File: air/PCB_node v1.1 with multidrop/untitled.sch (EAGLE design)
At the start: 100 parts, among them J1 10118193-0001LF, J2 10118193-0001LF, K1 351, K2 351, K3 SRD-05VDC-SL-C, Q1 MMBT3904, Q2 MMBT3904, Q3 12MHz, Q4 S9013, Q5 S9013, Q6 S9013, Q7 12MHz, Q8 MMBT3904, Q9 MMBT3904, U1 CH340G, U10 ADS1115IDGSR, U2 ESP32-WROOM-32D, U3 AMS1117, U4 PC817X2NIP0F, U5 PC817X2NIP0F, U6 PC817X2NIP0F, U7 CH340G, U8 AMS1117, U9 ESP32-WROOM-32D, X1 MSTBA2, X2 MSTBA2, X3 MSTBA4, X4 MSTBA3, X5 MSTBA2, X6 MSTBA4, X7 C-GRID-02-70543

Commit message: PCB dasmeter dengan multidop
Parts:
- added D13, D14, D15: US1M-13, US1M-13:US1M-13
- added K4: 351, relay:351
- added Q10: S9013, S9013:S9013
- added R21, R9: (no value), rcl:R-EU_0207/12
- added R22: 1k, rcl:R-US_M0805
- added R29, R31: 10k, rcl:R-US_M0805
- added R30: 560, rcl:R-US_M0805
- added U11: PC817X2NIP0F, PC817X2NIP0F:PC817X2NIP0F
- added X8: MSTBA2, con-phoenix-508:MSTBA2
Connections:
- removed net 24V++: K3.NO, R15.2, SUPER-STEPDOWN1.IN+, X2-2.1
- removed net M0: EBYTEE220-900T22D1.M0, EBYTEE220-900T22D1.M1, U2.IO18
- new net GND-BATT: K3.NO, X1-2.1, X2-1.1
- new net M1: EBYTEE220-900T22D1.M1, U9.IO5
- new net M2_RX: D14.A, K43.P, R30.2
- new net M2_SWITCHGPS: R22.2, U9.IO26
- new net M2_TX: K42.P, U9.IO16
- new net N$30: R22.1, U11.A
- new net N$31: Q10.B, U11.ET
- new net N$32: R29.2, U11.CT
- new net N$33: D13.A, K41.2, Q10.C
- new net N$34: D14.K, U9.IO17
- new net N$35: D15.K, U2.IO17
- new net PB-PWR: R9.2, X3-3.1
- net 24V+: now also R15.2, SUPER-STEPDOWN1.IN+, X1-1.1; no longer K3.COM, X1-2.1, X2-1.1
- net CONFIG_LORA: now also U9.IO25; no longer U2.IO5
- net CYBLE3: now also R21.2, R9.1; no longer X3-3.1
- net GND: now also EBYTEE220-900T22D1.M0, K3.COM, Q10.E, R21.1, U11.C, X2-2.1; no longer X1-1.1
- net OUT+: now also D13.K, K41.1, R29.1
- net RXLORA_MICRO: now also D15.A, R31.1; no longer U2.IO17
- net RX_GPS: now also K43.O; no longer U9.IO19
- net RX_LORA: now also K43.S
- net RX_MICRO: now also U9.IO18; no longer U9.IO16
- net SCL1: now also X8-1.1
- net SDA1: now also X8-2.1
- net TX_GPS: now also K42.O; no longer U9.IO18
- net TX_LORA: now also K42.S
- net TX_MICRO: now also U9.IO19; no longer U9.IO17
- net VCC: now also R31.2
- net VCC1: now also R30.1
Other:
- moved on the sheet: D11, D12, R19, R20, SV1, X7-1, X7-2

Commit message: menambah GPS chip
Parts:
- added C22: 27nH, rcl:C-EUC0805K
- added C23: 10nF, rcl:C-EUC0805K
- added D16: SML-LXT0805IW-TR, SML-LXT0805IW-TR:SML-LXT0805IW-TR
- added J3: U.FL-R-SMT(01), U.FL-R-SMT_01_:U.FL-R-SMT(01)
- added Q11: PDTC114EU,115, PDTC114EU_115:PDTC114EU,115
- added R32: 10, rcl:R-US_M0805
- added R33: 1k, rcl:R-US_M0805
- added U12: NEO-M8N-0, NEO-M8N-0:NEO-M8N-0
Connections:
- new net N$36: C22.1, C23.1, R32.2
- new net N$37: R32.1, U12.VCC_RF
- new net N$38: D16.C, Q11.OUTPUT
- new net N$39: D16.A, R33.1
- new net RF_IN: C22.2, J3.SIG, U12.RF_IN
- new net TIMEPULSE: Q11.INPUT, U12.TIMEPULSE
- net GND: now also C23.2, J3.GND, Q11.GND, U12.GND
- net RX_GPS: now also U12.RXD/SPI_MOSI
- net TX_GPS: now also U12.TXD/SPI_MISO
- net VCC1: now also R33.2, U12.VCC
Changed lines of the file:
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@@
 <part name="P+7" library="supply1" library_urn="urn:adsk.eagle:library:371" deviceset="VCC" device=""/>
 <part name="GND33" library="supply1" library_urn="urn:adsk.eagle:library:371" deviceset="GND" device=""/>
+<part name="U12" library="NEO-M8N-0" deviceset="NEO-M8N-0" device=""/>
+<part name="GND34" library="supply1" library_urn="urn:adsk.eagle:library:371" deviceset="GND" device=""/>
+<part name="J3" library="U.FL-R-SMT_01_" deviceset="U.FL-R-SMT(01)" device=""/>
+<part name="GND35" library="supply1" library_urn="urn:adsk.eagle:library:371" deviceset="GND" device=""/>
+<part name="C22" library="rcl" library_urn="urn:adsk.eagle:library:334" deviceset="C-EU" device="C0805K" package3d_urn="urn:adsk.eagle:package:23681/2" value="27nH"/>
+<part name="R32" library="rcl" library_urn="urn:adsk.eagle:library:334" deviceset="R-US_" device="M0805" package3d_urn="urn:adsk.eagle:package:23556/2" value="10"/>
+<part name="Q11" library="PDTC114EU_115" deviceset="PDTC114EU,115" device=""/>
+<part name="C23" library="rcl" library_urn="urn:adsk.eagle:library:334" deviceset="C-EU" device="C0805K" package3d_urn="urn:adsk.eagle:package:23681/2" value="10nF"/>
+<part name="GND36" library="supply1" library_urn="urn:adsk.eagle:library:371" deviceset="GND" device=""/>
+<part name="GND37" library="supply1" library_urn="urn:adsk.eagle:library:371" deviceset="GND" device=""/>
+<part name="D16" library="SML-LXT0805IW-TR" deviceset="SML-LXT0805IW-TR" device=""/>
+<part name="R33" library="rcl" library_urn="urn:adsk.eagle:library:334" deviceset="R-US_" device="M0805" package3d_urn="urn:adsk.eagle:package:23556/2" value="1k"/>
 </parts>
 <sheets>
@@
 <instance part="GND33" gate="1" x="78.74" y="172.72" smashed="yes">
 <attribute name="VALUE" x="76.2" y="170.18" size="1.778" layer="96"/>
+</instance>
+<instance part="U12" gate="G$1" x="287.02" y="99.06" smashed="yes">
+<attribute name="NAME" x="269.2361" y="122.4338" size="1.77845" layer="95"/>
+<attribute name="VALUE" x="269.2355" y="71.1126" size="1.77851875" layer="96"/>
+</instance>
+<instance part="GND34" gate="1" x="312.42" y="73.66" smashed="yes">
+<attribute name="VALUE" x="309.88" y="71.12" size="1.778" layer="96"/>
+</instance>
+<instance part="J3" gate="G$1" x="320.04" y="144.78" smashed="yes">
+<attribute name="NAME" x="316.22143125" y="148.85313125" size="1.27285" layer="95"/>
+<attribute name="VALUE" x="315.71218125" y="139.1793" size="1.27288125" layer="96"/>
+</instance>
+<instance part="GND35" gate="1" x="307.34" y="139.7" smashed="yes">
+<attribute name="VALUE" x="304.8" y="137.16" size="1.778" layer="96"/>
+</instance>
+<instance part="C22" gate="G$1" x="297.18" y="142.24" smashed="yes" rot="R180">
+<attribute name="NAME" x="295.656" y="141.859" size="1.778" layer="95" rot="R180"/>
+<attribute name="VALUE" x="295.656" y="146.939" size="1.778" layer="96" rot="R180"/>
+</instance>
+<instance part="R32" gate="G$1" x="297.18" y="132.08" smashed="yes" rot="R90">
+<attribute name="NAME" x="295.6814" y="128.27" size="1.778" layer="95" rot="R90"/>
+<attribute name="VALUE" x="300.482" y="128.27" size="1.778" layer="96" rot="R90"/>
+</instance>
+<instance part="Q11" gate="G$1" x="312.42" y="60.96" smashed="yes">
+<attribute name="NAME" x="304.7945" y="71.6357" size="2.54183125" layer="95"/>
+<attribute name="VALUE" x="304.79283125" y="47.7396" size="2.542390625" layer="96"/>
+</instance>
+<instance part="C23" gate="G$1" x="289.56" y="137.16" smashed="yes" rot="R270">
+<attribute name="NAME" x="289.941" y="135.636" size="1.778" layer="95" rot="R270"/>
+<attribute name="VALUE" x="284.861" y="135.636" size="1.778" layer="96" rot="R270"/>
+</instance>
+<instance part="GND36" gate="1" x="281.94" y="132.08" smashed="yes">
+<attribute name="VALUE" x="279.4" y="129.54" size="1.778" layer="96"/>
+</instance>
+<instance part="GND37" gate="1" x="322.58" y="48.26" smashed="yes">
+<attribute name="VALUE" x="320.04" y="45.72" size="1.778" layer="96"/>
+</instance>
+<instance part="D16" gate="G$1" x="322.58" y="78.74" smashed="yes" rot="R90">
+<attribute name="NAME" x="318.50973125" y="76.70486875" size="1.780740625" layer="95" rot="R90"/>
+<attribute name="VALUE" x="326.39315" y="76.70631875" size="1.77946875" layer="96" rot="R90"/>
+</instance>
+<instance part="R33" gate="G$1" x="322.58" y="96.52" smashed="yes" rot="R90">
+<attribute name="NAME" x="321.0814" y="92.71" size="1.778" layer="95" rot="R90"/>
+<attribute name="VALUE" x="325.882" y="92.71" size="1.778" layer="96" rot="R90"/>
 </instance>
 </instances>
@@
 <wire x1="91.44" y1="175.26" x2="78.74" y2="175.26" width="0.1524" layer="91"/>
 </segment>
+<segment>
+<pinref part="U12" gate="G$1" pin="GND"/>
+<wire x1="309.88" y1="76.2" x2="312.42" y2="76.2" width="0.1524" layer="91"/>
+<pinref part="GND34" gate="1" pin="GND"/>
+</segment>
+<segment>
+<pinref part="J3" gate="G$1" pin="GND"/>
+<wire x1="309.88" y1="142.24" x2="307.34" y2="142.24" width="0.1524" layer="91"/>
+<pinref part="GND35" gate="1" pin="GND"/>
+</segment>
+<segment>
+<pinref part="C23" gate="G$1" pin="2"/>
+<pinref part="GND36" gate="1" pin="GND"/>
+<wire x1="284.48" y1="137.16" x2="281.94" y2="137.16" width="0.1524" layer="91"/>
+<wire x1="281.94" y1="137.16" x2="281.94" y2="134.62" width="0.1524" layer="91"/>
+</segment>
+<segment>
+<pinref part="Q11" gate="G$1" pin="GND"/>
+<pinref part="GND37" gate="1" pin="GND"/>
+<wire x1="322.58" y1="53.34" x2="322.58" y2="50.8" width="0.1524" layer="91"/>
+</segment>
 </net>
 <net name="VUSB" class="0">
@@
 <label x="215.9" y="91.44" size="0.6096" layer="95" rot="R270" xref="yes"/>
 </segment>
+<segment>
+<pinref part="U12" gate="G$1" pin="VCC"/>
+<wire x1="309.88" y1="119.38" x2="312.42" y2="119.38" width="0.1524" layer="91"/>
+<label x="312.42" y="119.38" size="0.6096" layer="95" xref="yes"/>
+</segment>
+<segment>
+<pinref part="R33" gate="G$1" pin="2"/>
+<wire x1="322.58" y1="101.6" x2="322.58" y2="104.14" width="0.1524" layer="91"/>
+<label x="322.58" y="104.14" size="0.6096" layer="95" rot="R90" xref="yes"/>
+</segment>
 </net>
 <net name="RX_MICRO" class="0">
@@
 <label x="228.6" y="30.48" size="0.6096" layer="95" xref="yes"/>
 </segment>
+<segment>
+<pinref part="U12" gate="G$1" pin="RXD/SPI_MOSI"/>
+<wire x1="264.16" y1="93.98" x2="261.62" y2="93.98" width="0.1524" layer="91"/>
+<label x="261.62" y="93.98" size="0.6096" layer="95" rot="R180" xref="yes"/>
+</segment>
 </net>
 <net name="TX_GPS" class="0">
@@
 <wire x1="223.52" y1="45.72" x2="228.6" y2="45.72" width="0.1524" layer="91"/>
 <label x="228.6" y="45.72" size="0.6096" layer="95" xref="yes"/>
+</segment>
+<segment>
+<pinref part="U12" gate="G$1" pin="TXD/SPI_MISO"/>
+<wire x1="264.16" y1="91.44" x2="261.62" y2="91.44" width="0.1524" layer="91"/>
+<label x="261.62" y="91.44" size="0.6096" layer="95" rot="R180" xref="yes"/>
 </segment>
 </net>
@@
 </segment>
 </net>
+<net name="RF_IN" class="0">
+<segment>
+<pinref part="J3" gate="G$1" pin="SIG"/>
+<wire x1="309.88" y1="147.32" x2="297.18" y2="147.32" width="0.1524" layer="91"/>
+<pinref part="C22" gate="G$1" pin="2"/>
+<wire x1="297.18" y1="147.32" x2="292.1" y2="147.32" width="0.1524" layer="91"/>
+<junction x="297.18" y="147.32"/>
+<label x="292.1" y="147.32" size="0.6096" layer="95" rot="R180" xref="yes"/>
+</segment>
+<segment>
+<pinref part="U12" gate="G$1" pin="RF_IN"/>
+<wire x1="264.16" y1="104.14" x2="261.62" y2="104.14" width="0.1524" layer="91"/>
+<label x="261.62" y="104.14" size="0.6096" layer="95" rot="R180" xref="yes"/>
+</segment>
+</net>
+<net name="N$36" class="0">
+<segment>
+<pinref part="C22" gate="G$1" pin="1"/>
+<pinref part="R32" gate="G$1" pin="2"/>
+<wire x1="297.18" y1="139.7" x2="297.18" y2="137.16" width="0.1524" layer="91"/>
+<pinref part="C23" gate="G$1" pin="1"/>
+<wire x1="297.18" y1="137.16" x2="292.1" y2="137.16" width="0.1524" layer="91"/>
+<junction x="297.18" y="137.16"/>
+</segment>
+</net>
+<net name="N$37" class="0">
+<segment>
+<pinref part="R32" gate="G$1" pin="1"/>
+<pinref part="U12" gate="G$1" pin="VCC_RF"/>
+<wire x1="297.18" y1="127" x2="297.18" y2="109.22" width="0.1524" layer="91"/>
+<wire x1="297.18" y1="109.22" x2="309.88" y2="109.22" width="0.1524" layer="91"/>
+</segment>
+</net>
+<net name="TIMEPULSE" class="0">
+<segment>
+<pinref part="U12" gate="G$1" pin="TIMEPULSE"/>
+<wire x1="309.88" y1="104.14" x2="312.42" y2="104.14" width="0.1524" layer="91"/>
+<label x="312.42" y="104.14" size="0.6096" layer="95" xref="yes"/>
+</segment>
+<segment>
+<pinref part="Q11" gate="G$1" pin="INPUT"/>
+<wire x1="299.72" y1="63.5" x2="297.18" y2="63.5" width="0.1524" layer="91"/>
+<label x="297.18" y="63.5" size="0.6096" layer="95" rot="R180" xref="yes"/>
+</segment>
+</net>
+<net name="N$38" class="0">
+<segment>
+<pinref part="Q11" gate="G$1" pin="OUTPUT"/>
+<pinref part="D16" gate="G$1" pin="C"/>
+<wire x1="322.58" y1="68.58" x2="322.58" y2="71.12" width="0.1524" layer="91"/>
+</segment>
+</net>
+<net name="N$39" class="0">
+<segment>
+<pinref part="D16" gate="G$1" pin="A"/>
+<pinref part="R33" gate="G$1" pin="1"/>
+<wire x1="322.58" y1="88.9" x2="322.58" y2="91.44" width="0.1524" layer="91"/>
+</segment>
+</net>

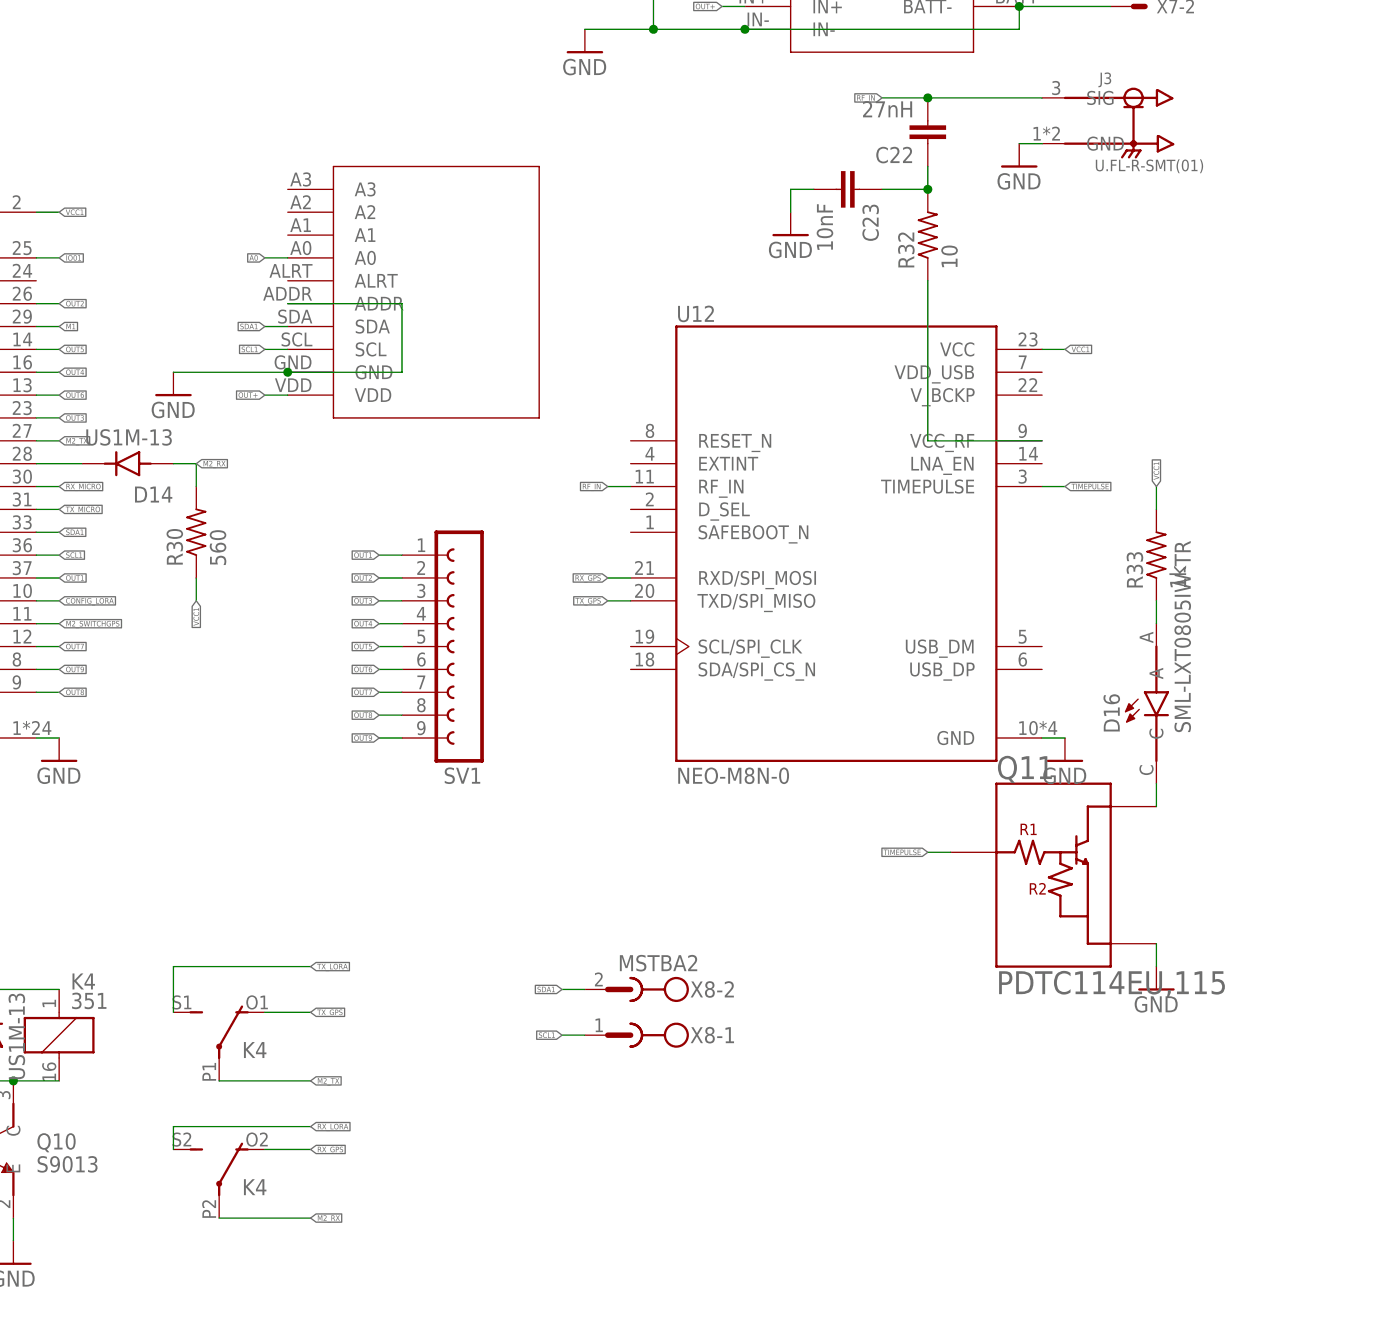
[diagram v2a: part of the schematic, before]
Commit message: PCB fix dasmeter
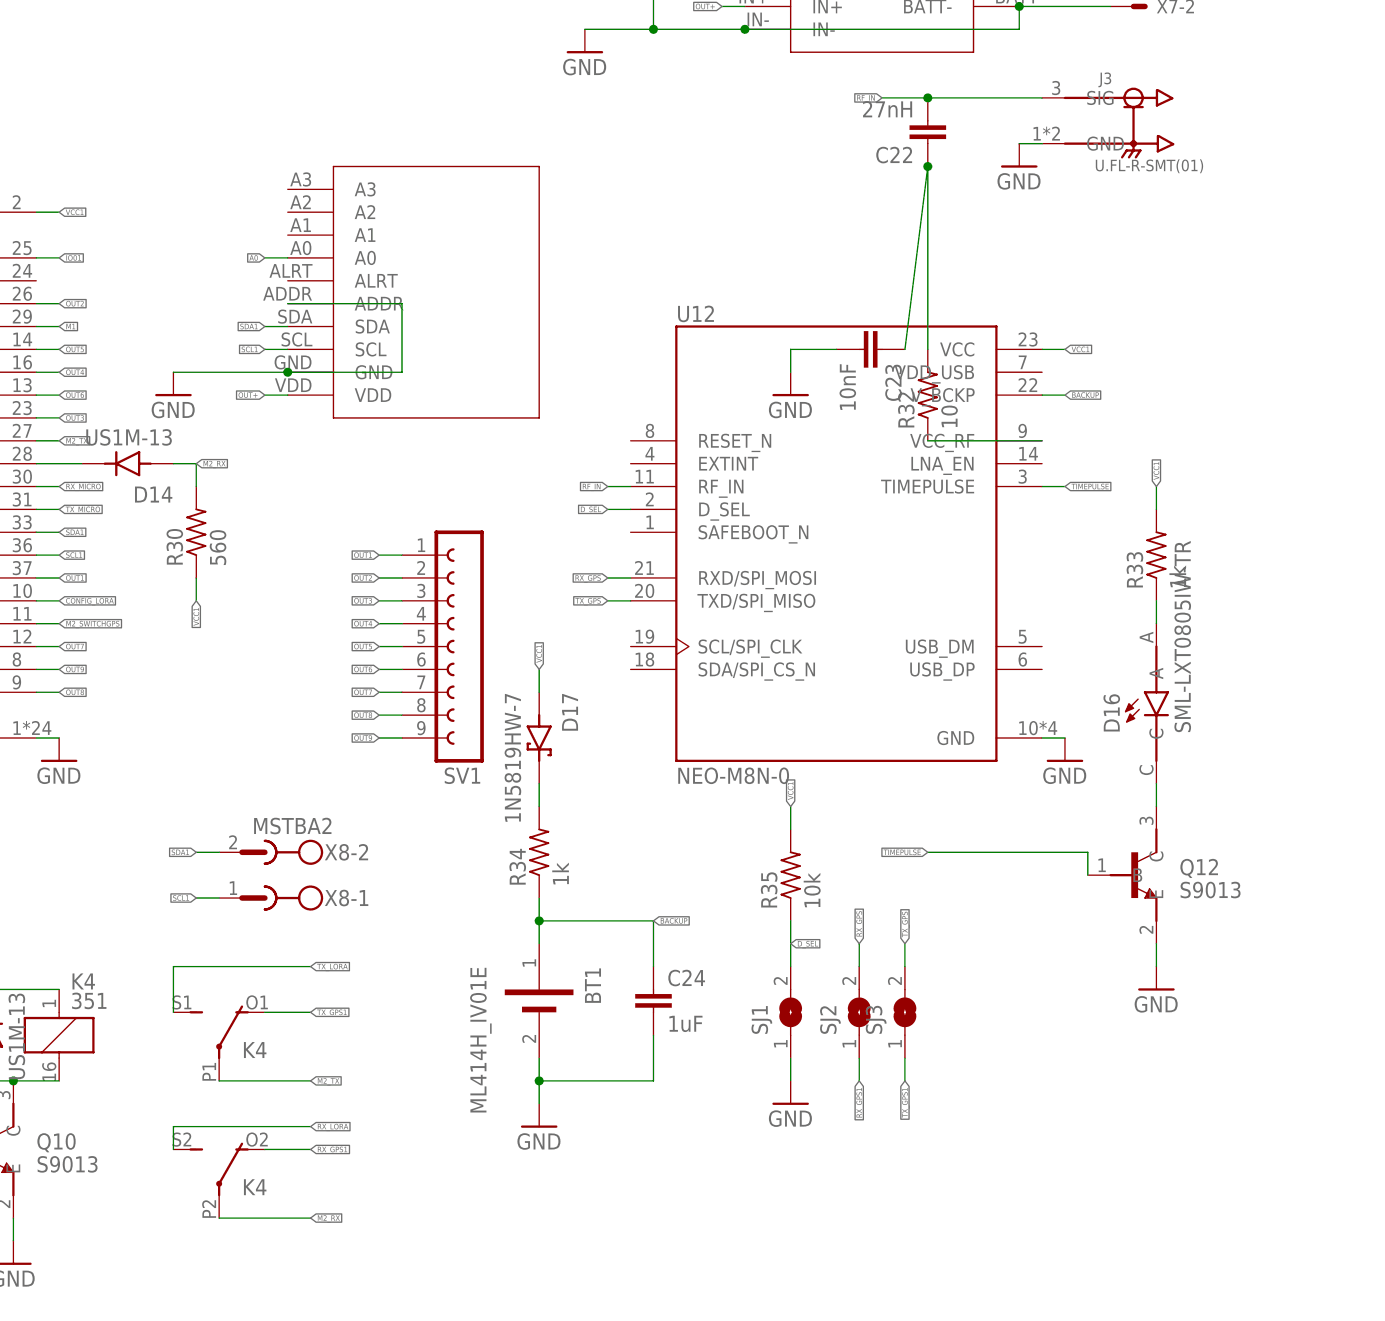
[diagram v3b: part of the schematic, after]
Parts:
- removed Q11: PDTC114EU,115, PDTC114EU_115:PDTC114EU,115
- added BT1: ML414H_IV01E, ML414H_IV01E:ML414H_IV01E
- added C24: 1uF, rcl:C-EUC0805K
- added D17: 1N5819HW-7, 1N5819HW-7:1N5819HW-7
- added Q12: S9013, S9013:S9013
- added R34: 1k, rcl:R-US_M0805
- added R35: 10k, rcl:R-US_M0805
- added SJ1, SJ2, SJ3: (no value), jumper:SJ
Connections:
- new net BACKUP: BT1.POS, C24.1, R34.1, U12.V_BCKP
- new net D_SEL: R35.1, SJ1.2, U12.D_SEL
- new net N$41: D17.K, R34.2
- new net RX_GPS1: K43.O, SJ2.1
- new net TX_GPS1: K42.O, SJ3.1
- net GND: now also BT1.NEG, C24.2, Q12.E, SJ1.1; no longer Q11.GND
- net N$38: now also Q12.C; no longer Q11.OUTPUT
- net RX_GPS: now also SJ2.2; no longer K43.O
- net TIMEPULSE: now also Q12.B; no longer Q11.INPUT
- net TX_GPS: now also SJ3.2; no longer K42.O
- net VCC1: now also D17.A, R35.2
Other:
- moved on the sheet: C23, R32, X8-1, X8-2

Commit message: scada air
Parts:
- removed MODUL-BATT1: (no value), MODUL-BATT:MODUL-BATT
- added D18: US1M-13, US1M-13:US1M-13
- added K5: 351, relay:351
- added Q11: S9013, S9013:S9013
- added R36: 1k, rcl:R-US_M0805
- added R37: 10k, rcl:R-US_M0805
- added U13: PC817X2NIP0F, PC817X2NIP0F:PC817X2NIP0F
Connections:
- new net M2_BATT-BACK-SWITCH: R36.2, U9.IO2
- new net N$40: R37.2, U13.CT
- new net N$42: D18.A, K51.2, Q11.C
- new net N$43: Q11.B, U13.ET
- new net N$44: K52.S, X7-2.S
- net GND: now also Q11.E, U13.C, X7-1.S; no longer MODUL-BATT1.BATT-, MODUL-BATT1.IN-, MODUL-BATT1.OUT-, X7-2.S
- net N$29: now also R36.1, U13.A; no longer MODUL-BATT1.BATT+, X7-1.S
- net OUT+: now also D18.K, K51.1, R37.1; no longer MODUL-BATT1.IN+
- net OUT-BATT: now also K52.P; no longer MODUL-BATT1.OUT+
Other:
- moved on the sheet: X7-1, X7-2
